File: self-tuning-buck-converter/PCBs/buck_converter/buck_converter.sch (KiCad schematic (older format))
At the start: 18 parts

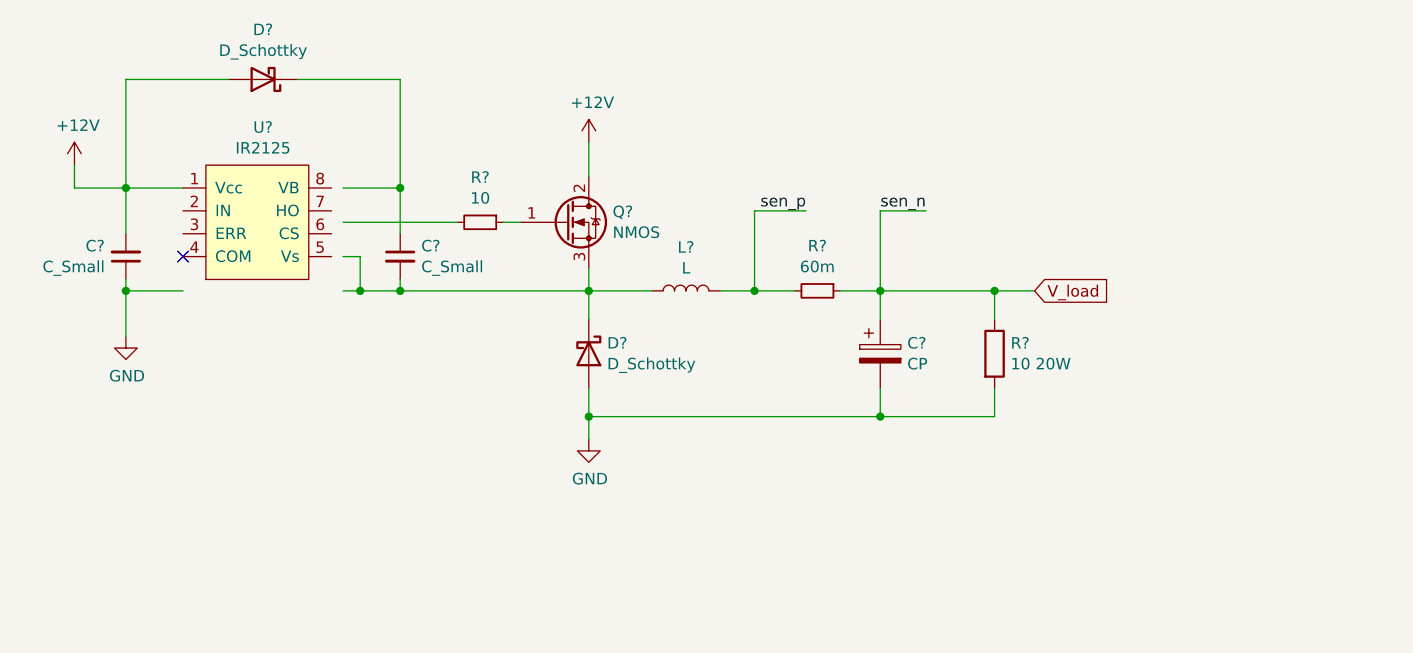
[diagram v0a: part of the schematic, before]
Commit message: update gate driver schematic
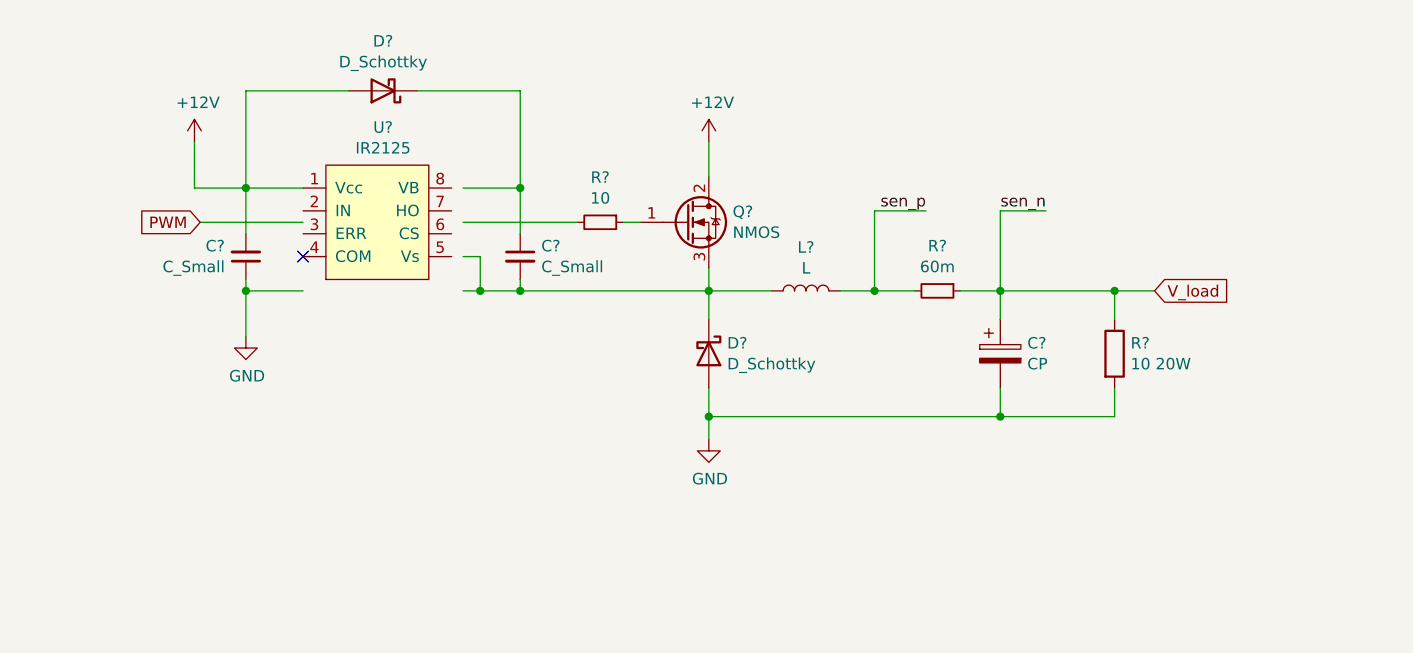
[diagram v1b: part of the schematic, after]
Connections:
- wire segments 67 -> 68
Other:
- moved on the sheet: C?, D?, L?, Q?, R?, U?

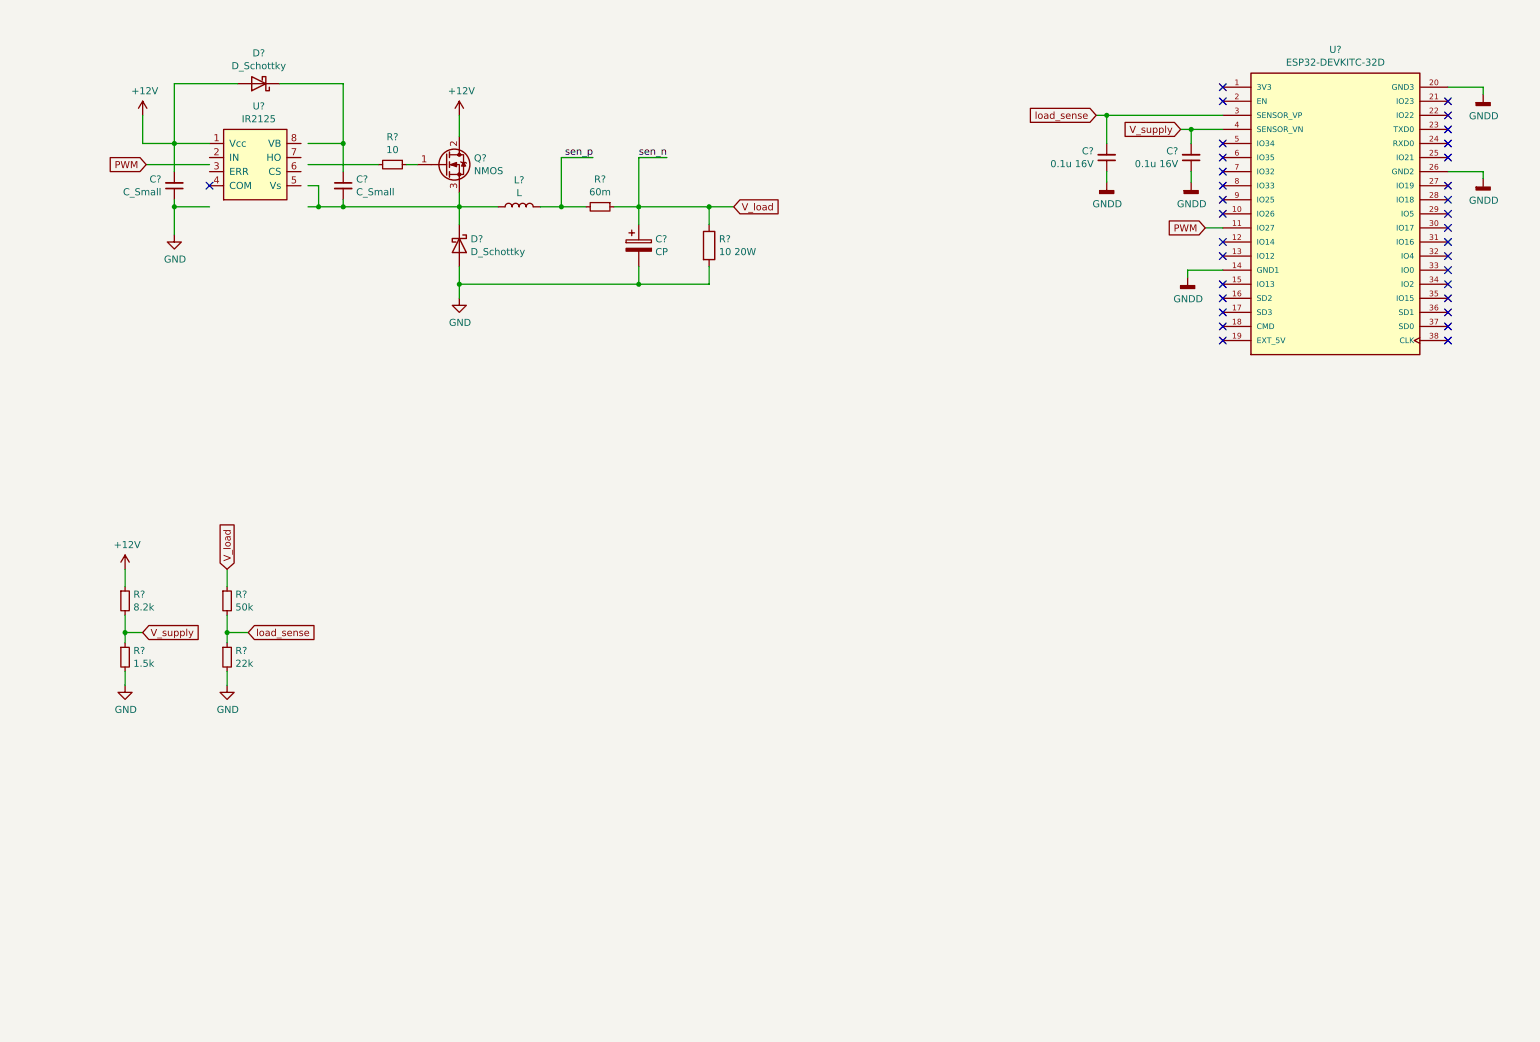
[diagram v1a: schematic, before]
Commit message: updated pcb schematic, added the current sense amplifier, ripple averager (low pass filter), and ripple peak detector
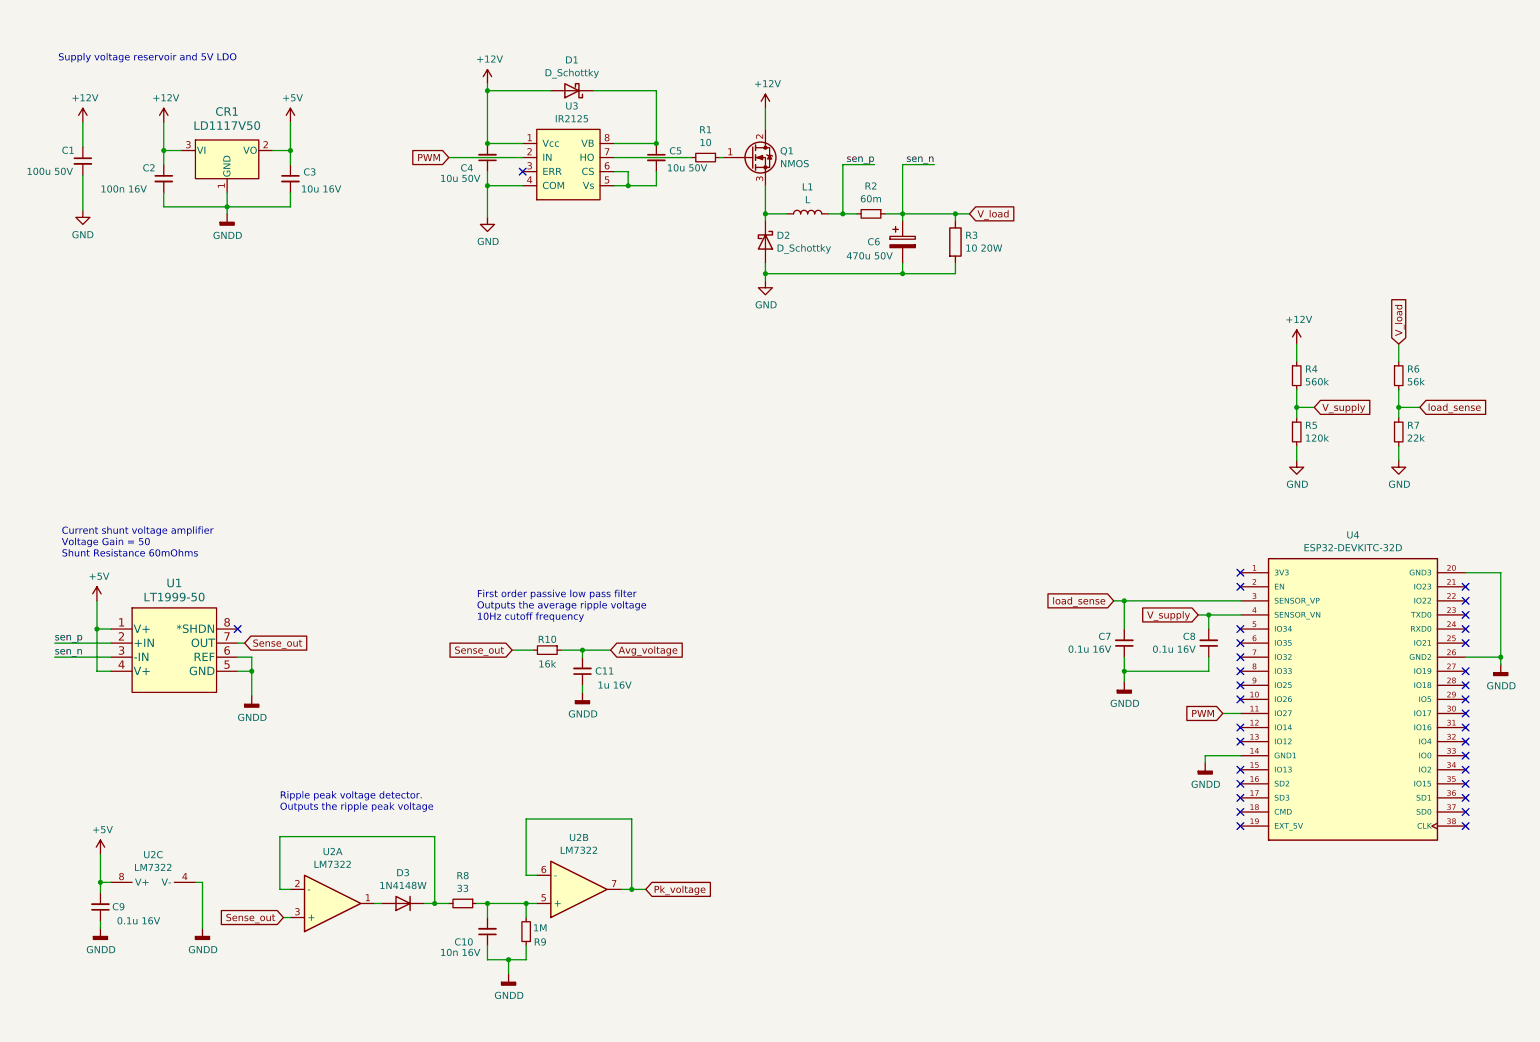
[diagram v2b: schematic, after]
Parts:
- removed C?: CP, symbol Device:CP
- added C1: 100u 50V, symbol Device:C_Small
- added C10: 10n 16V, symbol Device:C_Small
- added C11: 1u 16V, symbol Device:C_Small
- added C2: 100n 16V, symbol Device:C_Small
- added C3: 10u 16V, symbol Device:C_Small
- added C6: 470u 50V, symbol Device:CP
- added C9: 0.1u 16V, symbol Device:C_Small
- added CR1: LD1117V50, TO-220_STM, symbol LD1117V50:LD1117V50
- added D3: 1N4148W, Diode_SMD:D_SOD-123, symbol Diode:1N4148W
- added R10: 16k, Resistor_SMD:R_0603_1608Metric_Pad0.98x0.95mm_HandSolder, symbol Device:R_Small
- added R8: 33, symbol Device:R_Small
- added R9: 1M, symbol Device:R_Small
- added U1: LT1999-50, MSOP_8_ADI, symbol LT1999-50:LT1999MPMS8-50-PBF
- added U2: LM7322, symbol Device:Opamp_Dual_Generic
- C4, C5: renamed from C?; value C_Small -> 10u 50V
- R4: renamed from R?; value 8.2k -> 560k
- R5: renamed from R?; value 1.5k -> 120k
- R6: renamed from R?; value 50k -> 56k
- gave numbers to parts that had none: 12
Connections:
- net labels added: +5V, Avg_voltage, Pk_voltage, Sense_out
- wire segments 68 -> 126
- no-connect marks 33 -> 34
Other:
- note added: "Current shunt voltage amplifier\nVoltage Gain = 50\nShunt Resistance 60mOhms"
- note added: "First order passive low pass filter\nOutputs the average ripple voltage\n10Hz cutoff frequency"
- note added: "Ripple peak voltage detector.\nOutputs the ripple peak voltage"
- note added: "Supply voltage reservoir and 5V LDO"
- moved on the sheet: C4, C5, C7, C8, D1, D2, L1, Q1, R1, R2, R3, R4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
